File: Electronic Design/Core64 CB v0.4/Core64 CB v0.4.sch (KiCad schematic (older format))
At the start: 36 parts, among them J1 TSM-116-03-T-SV‎, J2 TSM-116-03-T-SV‎, U10 TS3A4751PWR, U11 TS3A4751PWR, U5 SI7210-B-01, U6 SI7210-B-02, U7 SI7210-B-03, U8 SI7210-B-04, U9 LTR-329ALS-01, X1 SFH11-NBPC-D03-ST-BK

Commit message: Complete draft of Core Board with updated Core64 Logo
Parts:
- removed L2: Core_64_Logo, Core_Memory_8x8_Array:Core64_Logo, symbol CORE_64_LIBRARY:Core_64_Logo
- added L1: Core_64_Logo_9mm_tall, Core_Memory_8x8_Array:Core64_Logo_9mm_tall, symbol CORE_64_LIBRARY:Core_64_Logo_9mm_tall
- renumbered L1 to L2
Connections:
- net labels added: SAO_GPIO1, SAO_GPIO2
- net labels removed: SAO3_GPIO1, SAO3_GPIO2
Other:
- note added: "SILKSCREEN: \nSAO, GND, 3V3, SDA,SCL\nL1GPIO1, L2GPIO2"
- note added: "SILKSCREEN:\nXT3,7\nXT2,6\nXT1,5\nXT0,4\nXB0\nXB1\nXB2\nXB3\nXB4\nXB5\nXB6\nXB7\nL1GPIO1\nL2GPIO2\nLAYER3\nLAYER4"
- note removed: "SILKSCREEN: L1_GPIO1, L2_GPIO2"
- note removed: "SILKSCREEN:\nXT3,7\nXT2,6\nXT1,5\nXT0,4\nXB0\nXB1\nXB2\nXB3\nXB4\nXB5\nXB6\nXB7\nL1_GPIO1\nL2_GPIO2\nLAYER3\nLAYER4"
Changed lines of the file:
@@
 $EndComp
 Text Notes 7300 2600 0    50   ~ 0
-SILKSCREEN:\nXT3,7\nXT2,6\nXT1,5\nXT0,4\nXB0\nXB1\nXB2\nXB3\nXB4\nXB5\nXB6\nXB7\nL1_GPIO1\nL2_GPIO2\nLAYER3\nLAYER4
+SILKSCREEN:\nXT3,7\nXT2,6\nXT1,5\nXT0,4\nXB0\nXB1\nXB2\nXB3\nXB4\nXB5\nXB6\nXB7\nL1GPIO1\nL2GPIO2\nLAYER3\nLAYER4
 $Comp
 L CORE_64_LIBRARY:Core_Memory_8x8_Array_Front_Facing CM1
@@
 $EndComp
 Text GLabel 9300 1800 2    50   Input ~ 0
-SAO3_GPIO1
+SAO_GPIO1
 Text GLabel 9300 2950 2    50   Input ~ 0
-SAO3_GPIO2
+SAO_GPIO2
 Text GLabel 8850 1800 0    50   Input ~ 0
 3V3_800mA
@@
 	9150 1800 9300 1800
 Text GLabel 6950 2800 2    50   Input ~ 0
-SAO3_GPIO2
+SAO_GPIO2
 Text GLabel 6950 2950 2    50   Input ~ 0
-SAO3_GPIO1
+SAO_GPIO1
 Wire Wire Line
 	6850 2800 6950 2800
@@
 	6950 2950 6650 2950
 $Comp
-L CORE_64_LIBRARY:Core_64_Github_Link L1
+L CORE_64_LIBRARY:Core_64_Github_Link L2
 U 1 1 5E9833FF
 P 4850 7800
-F 0 "L1" H 4875 7847 50  0000 L CNN
+F 0 "L2" H 4875 7847 50  0000 L CNN
 F 1 "Core_64_Github_Link" H 4875 7754 50  0000 L CNN
 F 2 "Core_Memory_8x8_Array:Github_Link" H 4850 7800 50  0001 C CNN
@@
 	6350 2650 6950 2650
 Text Notes 9150 1700 0    50   ~ 0
-SILKSCREEN: L1_GPIO1, L2_GPIO2
+SILKSCREEN: \nSAO, GND, 3V3, SDA,SCL\nL1GPIO1, L2GPIO2
 $Comp
 L Device:C C13
@@
 Text Notes 550  7900 0    50   ~ 0
 CORE BOARD   V0.4   2020-08-20   A. GEPPERT   WWW.MACHINEIDEAS.COM\nInteractive Core Memory
-$Comp
-L CORE_64_LIBRARY:Core_64_Logo L2
-U 1 1 5F5DF542
-P 3950 7800
-F 0 "L2" H 3975 7847 50  0000 L CNN
-F 1 "Core_64_Logo" H 3975 7754 50  0000 L CNN
-F 2 "Core_Memory_8x8_Array:Core64_Logo" H 3950 7800 50  0001 C CNN
-F 3 "" H 3950 7800 50  0001 C CNN
-	1    3950 7800
-	1    0    0    -1
-$EndComp
 $Comp
 L power:GNDD #PWR0102
@@
 Text Notes 3650 5550 0    50   ~ 0
 STEP 3:\nAdd two quad switches and two decoupling caps.
+$Comp
+L CORE_64_LIBRARY:Core_64_Logo_9mm_tall L1
+U 1 1 5F3DC9AF
+P 3850 7800
+F 0 "L1" H 3875 7847 50  0000 L CNN
+F 1 "Core_64_Logo_9mm_tall" H 3875 7754 50  0000 L CNN
+F 2 "Core_Memory_8x8_Array:Core64_Logo_9mm_tall" H 3850 7800 50  0001 C CNN
+F 3 "" H 3850 7800 50  0001 C CNN
+	1    3850 7800
+	1    0    0    -1
+$EndComp
 $EndSCHEMATC

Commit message: Update Core 64 logo
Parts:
- removed L2: Core_64_Github_Link, Core_Memory_8x8_Array:Github_Link, symbol CORE_64_LIBRARY:Core_64_Github_Link
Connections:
- net LAYER_1 renamed PLANE_1
- net LAYER_2 renamed PLANE_2
- net LAYER_3 renamed PLANE_3
- net LAYER_4 renamed PLANE_4
- net LAYER_5 renamed PLANE_5
- net LAYER_6 renamed PLANE_6
- net LAYER_7 renamed PLANE_7
- net LAYER_8 renamed PLANE_8
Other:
- note added: "CORE BOARD V0.4 [REL. DATE] A. GEPPERT Core64.MachineIdeas.com\nInteractive Core Memory"
- note added: "SILKSCREEN: \nSAO, GND, 3V3, SDA,SCL\nP1/GPIO1, P2/GPIO2"
- note added: "SILKSCREEN:\nXT3,7\nXT2,6\nXT1,5\nXT0,4\nXB0\nXB1\nXB2\nXB3\nXB4\nXB5\nXB6\nXB7\nP1/IO1\nP2/IO2\nP3\nP4"
- note added: "SILKSCREEN:\nYL0\nYL1\nYL2\nYL3\nYL4,6\nYL5,7\nSEN1\nSEN2\nSCL\nSDA\n3V3\nGNDD\nP8\nP7\nP6\nP5"
- note added: "STEP 2:\nSolder one plane SJ."
- note added: "STEP 3:\nInstall two quad switches and two decoupling caps."
- note added: "STEP 4 (LOGIC BOARD):\nCut and solder two plane select/SAO-GPIO jumpers."
- note added: "[OPTIONAL] CORE PLANE SELECT"
- note removed: "CORE BOARD V0.4 2020-08-20 A. GEPPERT WWW.MACHINEIDEAS.COM\nInteractive Core Memory"
- note removed: "SILKSCREEN: \nSAO, GND, 3V3, SDA,SCL\nL1GPIO1, L2GPIO2"
- note removed: "SILKSCREEN:\nXT3,7\nXT2,6\nXT1,5\nXT0,4\nXB0\nXB1\nXB2\nXB3\nXB4\nXB5\nXB6\nXB7\nL1GPIO1\nL2GPIO2\nLAYER3\nLAYER4"
- note removed: "SILKSCREEN:\nYL0\nYL1\nYL2\nYL3\nYL4,6\nYL5,7\nSEN1\nSEN2\nSCL\nSDA\n3V3\nGNDD\nLAYER8\nLAYER7\nLAYER6\nLAYER5"
- note removed: "STEP 2:\nSolder one layer SJ."
- note removed: "STEP 3:\nAdd two quad switches and two decoupling caps."
- note removed: "[OPTIONAL] MATIX LAYER ACTIVATION"
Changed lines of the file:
@@
 	2150 1700 2050 1700
 Text Notes 1150 2650 2    50   ~ 0
-SILKSCREEN:\nYL0\nYL1\nYL2\nYL3\nYL4,6\nYL5,7\nSEN1\nSEN2\nSCL\nSDA\n3V3\nGNDD\nLAYER8\nLAYER7\nLAYER6\nLAYER5
+SILKSCREEN:\nYL0\nYL1\nYL2\nYL3\nYL4,6\nYL5,7\nSEN1\nSEN2\nSCL\nSDA\n3V3\nGNDD\nP8\nP7\nP6\nP5
 Wire Wire Line
 	2050 1700 1500 1700
@@
 $EndComp
 Text Notes 7300 2600 0    50   ~ 0
-SILKSCREEN:\nXT3,7\nXT2,6\nXT1,5\nXT0,4\nXB0\nXB1\nXB2\nXB3\nXB4\nXB5\nXB6\nXB7\nL1GPIO1\nL2GPIO2\nLAYER3\nLAYER4
+SILKSCREEN:\nXT3,7\nXT2,6\nXT1,5\nXT0,4\nXB0\nXB1\nXB2\nXB3\nXB4\nXB5\nXB6\nXB7\nP1/IO1\nP2/IO2\nP3\nP4
 $Comp
 L CORE_64_LIBRARY:Core_Memory_8x8_Array_Front_Facing CM1
@@
 Wire Wire Line
 	6950 2950 6650 2950
-$Comp
-L CORE_64_LIBRARY:Core_64_Github_Link L2
-U 1 1 5E9833FF
-P 4850 7800
-F 0 "L2" H 4875 7847 50  0000 L CNN
-F 1 "Core_64_Github_Link" H 4875 7754 50  0000 L CNN
-F 2 "Core_Memory_8x8_Array:Github_Link" H 4850 7800 50  0001 C CNN
-F 3 "" H 4850 7800 50  0001 C CNN
-	1    4850 7800
-	1    0    0    -1
-$EndComp
 Text Notes 6350 6900 0    50   ~ 0
 Work in progress
@@
 	6350 2650 6950 2650
 Text Notes 9150 1700 0    50   ~ 0
-SILKSCREEN: \nSAO, GND, 3V3, SDA,SCL\nL1GPIO1, L2GPIO2
+SILKSCREEN: \nSAO, GND, 3V3, SDA,SCL\nP1/GPIO1, P2/GPIO2
 $Comp
 L Device:C C13
@@
 	8600 4550 9950 4550
 Text Notes 550  5300 0    100  ~ 0
-[OPTIONAL] MATIX LAYER ACTIVATION
+[OPTIONAL] CORE PLANE SELECT
 Text Notes 2800 1650 0    50   ~ 0
 SILKSCREEN:\nPixel 0-7 ->
@@
 SILKSCREEN:\nPixel 56-63->
 Text Notes 550  7900 0    50   ~ 0
-CORE BOARD   V0.4   2020-08-20   A. GEPPERT   WWW.MACHINEIDEAS.COM\nInteractive Core Memory
+CORE BOARD   V0.4   [REL. DATE]   A. GEPPERT   Core64.MachineIdeas.com\nInteractive Core Memory
 $Comp
 L power:GNDD #PWR0102
@@
 Ceramic
 Text GLabel 1900 2400 2    50   Output ~ 0
-LAYER_8
+PLANE_8
 Text GLabel 1900 2500 2    50   Output ~ 0
-LAYER_7
+PLANE_7
 Text GLabel 1900 2600 2    50   Output ~ 0
-LAYER_6
+PLANE_6
 Text GLabel 1900 2700 2    50   Output ~ 0
-LAYER_5
+PLANE_5
 Text GLabel 6350 2650 0    50   Output ~ 0
-LAYER_4
+PLANE_4
 Text GLabel 6350 2550 0    50   Output ~ 0
-LAYER_3
+PLANE_3
 Text GLabel 6350 2450 0    50   Output ~ 0
-LAYER_2
+PLANE_2
 Text GLabel 6350 2350 0    50   Output ~ 0
-LAYER_1
+PLANE_1
 Wire Wire Line
 	6950 2350 6650 2350
@@
 Connection ~ 2450 5700
 Text GLabel 2150 6500 0    50   Output ~ 0
-LAYER_5
+PLANE_5
 Text GLabel 2150 6700 0    50   Output ~ 0
-LAYER_6
+PLANE_6
 Text GLabel 2150 6900 0    50   Output ~ 0
-LAYER_7
+PLANE_7
 Text GLabel 2150 7100 0    50   Output ~ 0
-LAYER_8
+PLANE_8
 Text GLabel 2150 5700 0    50   Output ~ 0
-LAYER_1
+PLANE_1
 Text GLabel 2150 5900 0    50   Output ~ 0
-LAYER_2
+PLANE_2
 Text GLabel 2150 6100 0    50   Output ~ 0
-LAYER_3
+PLANE_3
 Text GLabel 2150 6300 0    50   Output ~ 0
-LAYER_4
+PLANE_4
 $Comp
 L TI_TS3A4751PWR:TS3A4751PWR U10
@@
 STEP 1:\nCut all header-to-matrix SJs.
 Text Notes 1950 5550 0    50   ~ 0
-STEP 2:\nSolder one layer SJ.
-Text Notes 3650 5550 0    50   ~ 0
-STEP 3:\nAdd two quad switches and two decoupling caps.
+STEP 2:\nSolder one plane SJ.
+Text Notes 3050 5550 0    50   ~ 0
+STEP 3:\nInstall two quad switches and two decoupling caps.
+Text Notes 5250 5550 0    50   ~ 0
+STEP 4 (LOGIC BOARD):\nCut and solder two plane select/SAO-GPIO jumpers.
 $Comp
 L CORE_64_LIBRARY:Core_64_Logo_9mm_tall L1
 U 1 1 5F3DC9AF
-P 3850 7800
-F 0 "L1" H 3875 7847 50  0000 L CNN
-F 1 "Core_64_Logo_9mm_tall" H 3875 7754 50  0000 L CNN
-F 2 "Core_Memory_8x8_Array:Core64_Logo_9mm_tall" H 3850 7800 50  0001 C CNN
-F 3 "" H 3850 7800 50  0001 C CNN
-	1    3850 7800
-	1    0    0    -1
-$EndComp
+P 3900 7800
+F 0 "L1" H 3925 7847 50  0000 L CNN
+F 1 "Core_64_Logo_9mm_tall" H 3925 7754 50  0000 L CNN
+F 2 "Core_Memory_8x8_Array:Core64_Logo_9mm_tall" H 3900 7800 50  0001 C CNN
+F 3 "" H 3900 7800 50  0001 C CNN
+	1    3900 7800
+	1    0    0    -1
+$EndComp

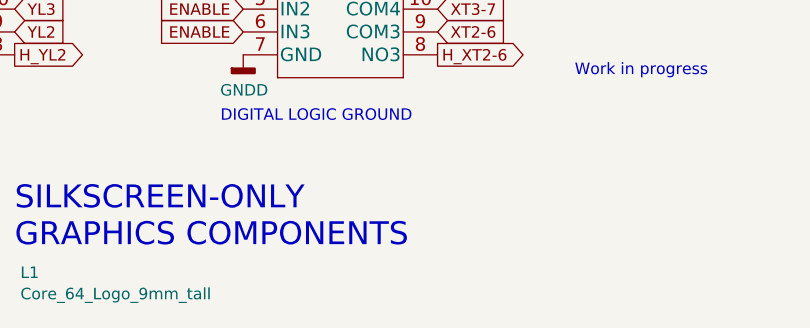
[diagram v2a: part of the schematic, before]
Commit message: Add Mode - + Set button in Commodore font, clean-up silk screen, solder mask between 16x T.H. and pads
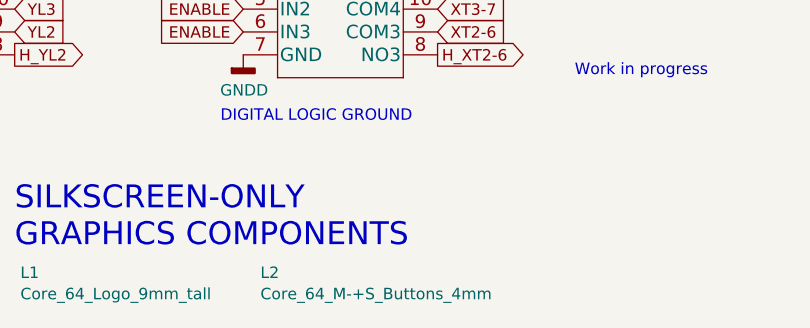
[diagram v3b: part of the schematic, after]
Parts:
- added L2: Core_64_M-+S_Buttons_4mm, Core_Memory_8x8_Array:Core64-M_-_+_S_Buttons, symbol CORE_64_LIBRARY:Core_64_M-+S_Buttons_4mm
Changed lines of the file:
@@
+	1    0    0    -1
+$EndComp
+$Comp
+L CORE_64_LIBRARY:Core_64_M-+S_Buttons_4mm L2
+U 1 1 5F41CA57
+P 4950 7800
+F 0 "L2" H 4975 7847 50  0000 L CNN
+F 1 "Core_64_M-+S_Buttons_4mm" H 4975 7754 50  0000 L CNN
+F 2 "Core_Memory_8x8_Array:Core64-M_-_+_S_Buttons" H 4950 7800 50  0001 C CNN
+F 3 "" H 4950 7800 50  0001 C CNN
+	1    4950 7800
 	1    0    0    -1
 $EndComp

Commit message: CB V0.4 as prototype and BOM parts ordered
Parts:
- JP1, JP2, JP3, JP4, JP5, JP6, JP7, JP8: footprint Jumper:SolderJumper-2_P1.3mm_Bridged_RoundedPad1.0x1.5mm -> Jumper:SolderJumper-2_P1.3mm_Open_Pad1.0x1.5mm; symbol Jumper:SolderJumper_2_Bridged -> Jumper:SolderJumper_2_Open
- renumbered C9 to C1, C10 to C2, C11 to C3, C12 to C4, C13 to C5, C1 to C6, C2 to C7, U5 to U1, U6 to U2, U7 to U3, U8 to U4, U9 to U5, U10 to U6, U11 to U7
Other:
- note added: "AS PROTOTYPED 22AUG2020"
- note added: "CORE BOARD V0.4 [REL. DATE]. ANDY GEPPERT \nCore64.MachineIdeas.com\nInteractive Core Memory"
- note added: "DEFAULT FOR ONE CORE PLANE ONLY"
- note added: "SILKSCREEN FRONT AND BACK: \nSAO, GNDD, 3V3, SDA,SCL\nGPIO1, GPIO2"
- note added: "SILKSCREEN GRAPHICS"
- note added: "SILKSCREEN: 0x30"
- note added: "SILKSCREEN: 0x31"
- note added: "SILKSCREEN: 0x32"
- note added: "SILKSCREEN: 0x33"
- note added: "STEP 1: Do NOT solder\nany JP1 through JP8."
- note added: "STEP 1: Solder all eight header-to-matrix SJs.\nJP1 through JP8."
- note added: "STEP 2: Do NOT solder\nany JP9 through JP16."
- note added: "STEP 2: Solder ONE \nplane JP9 to JP16."
- note added: "STEP 3:\nNo additional components needed."
- note added: "STEP 4 (LOGIC BOARD):\nSee instructions on Logic Board."
- note removed: "CORE BOARD V0.4 [REL. DATE] A. GEPPERT Core64.MachineIdeas.com\nInteractive Core Memory"
- note removed: "SILKSCREEN-ONLY\nGRAPHICS COMPONENTS"
- note removed: "SILKSCREEN: HS1 I2C 0x30"
- note removed: "SILKSCREEN: HS1 I2C 0x31"
- note removed: "SILKSCREEN: HS1 I2C 0x32"
- note removed: "SILKSCREEN: HS1 I2C 0x33"
- note removed: "SILKSCREEN: \nSAO, GND, 3V3, SDA,SCL\nP1/GPIO1, P2/GPIO2"
- note removed: "SILKSCREEN: “+”"
- note removed: "SILKSCREEN: “-“"
- note removed: "SILKSCREEN: “M”"
- note removed: "SILKSCREEN: “S”"
- note removed: "STEP 1:\nCut all header-to-matrix SJs."
- note removed: "STEP 2:\nSolder one plane SJ."
- note removed: "STEP 4 (LOGIC BOARD):\nCut and solder two plane select/SAO-GPIO jumpers."
- note removed: "Work in progress"
- moved on the sheet: C1, C2, C3, C4, C5, C6, C7, CM1, J1, J2, JP10, JP11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

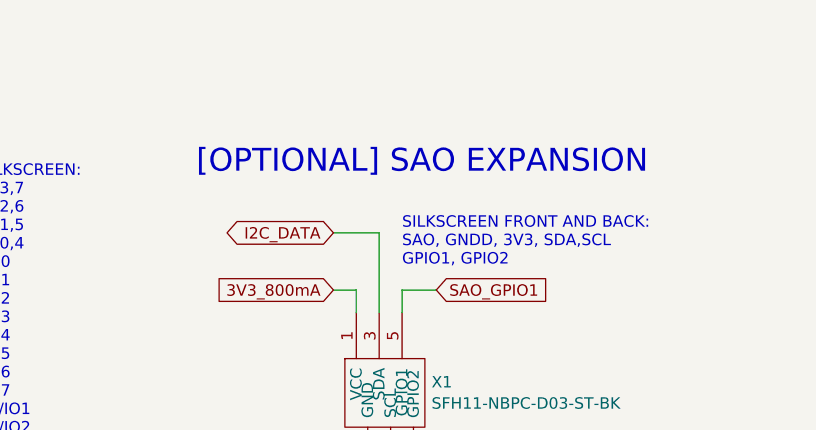
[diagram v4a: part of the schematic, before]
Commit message: Update Simple Add Ons #2 on all schematics PCBs
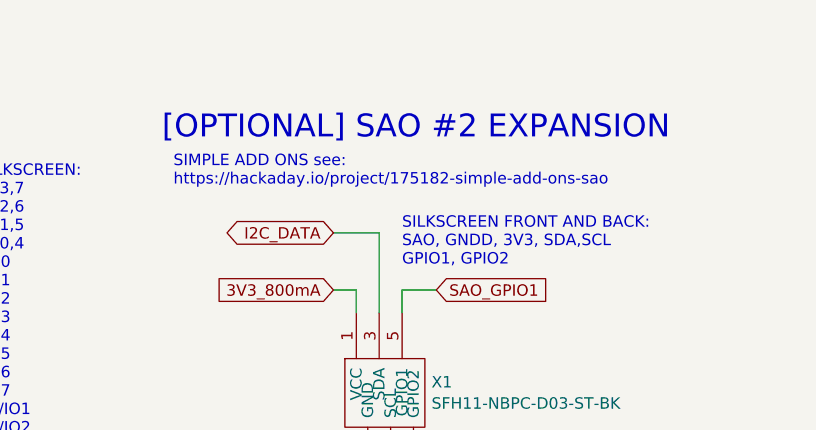
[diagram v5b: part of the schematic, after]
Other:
- note added: "SIMPLE ADD ONS see:\nhttps://hackaday.io/project/175182-simple-add-ons-sao"
- note added: "[OPTIONAL] SAO #2 EXPANSION"
- note removed: "[OPTIONAL] SAO EXPANSION"
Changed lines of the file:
@@
 Date "2020-08-22"
 Rev "0.4"
-Comp "Andy Geppert - Machine Ideas, LLC"
-Comment1 ""
-Comment2 ""
+Comp "Core64.MachineIdeas.com"
+Comment1 "As prototyped 22AUG2020"
+Comment2 "Andy Geppert"
 Comment3 ""
 Comment4 ""
@@
 Text Notes 600  700  0    100  ~ 0
 CORE MATRIX
-Text Notes 8250 1200 0    100  ~ 0
-[OPTIONAL] SAO EXPANSION
+Text Notes 8100 1050 0    100  ~ 0
+[OPTIONAL] SAO #2 EXPANSION
 Text Notes 1600 3200 0    50   ~ 0
 SILKSCREEN: 0x30
@@
 Text Notes 6350 6900 0    50   ~ 0
 AS PROTOTYPED 22AUG2020
+Text Notes 8150 1250 0    50   ~ 0
+SIMPLE ADD ONS see:\nhttps://hackaday.io/project/175182-simple-add-ons-sao
 $EndSCHEMATC
